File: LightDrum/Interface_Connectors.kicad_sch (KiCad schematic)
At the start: 6 parts, among them J1201 0525593652, J1202 0541323662, J1203 PWR-CONN

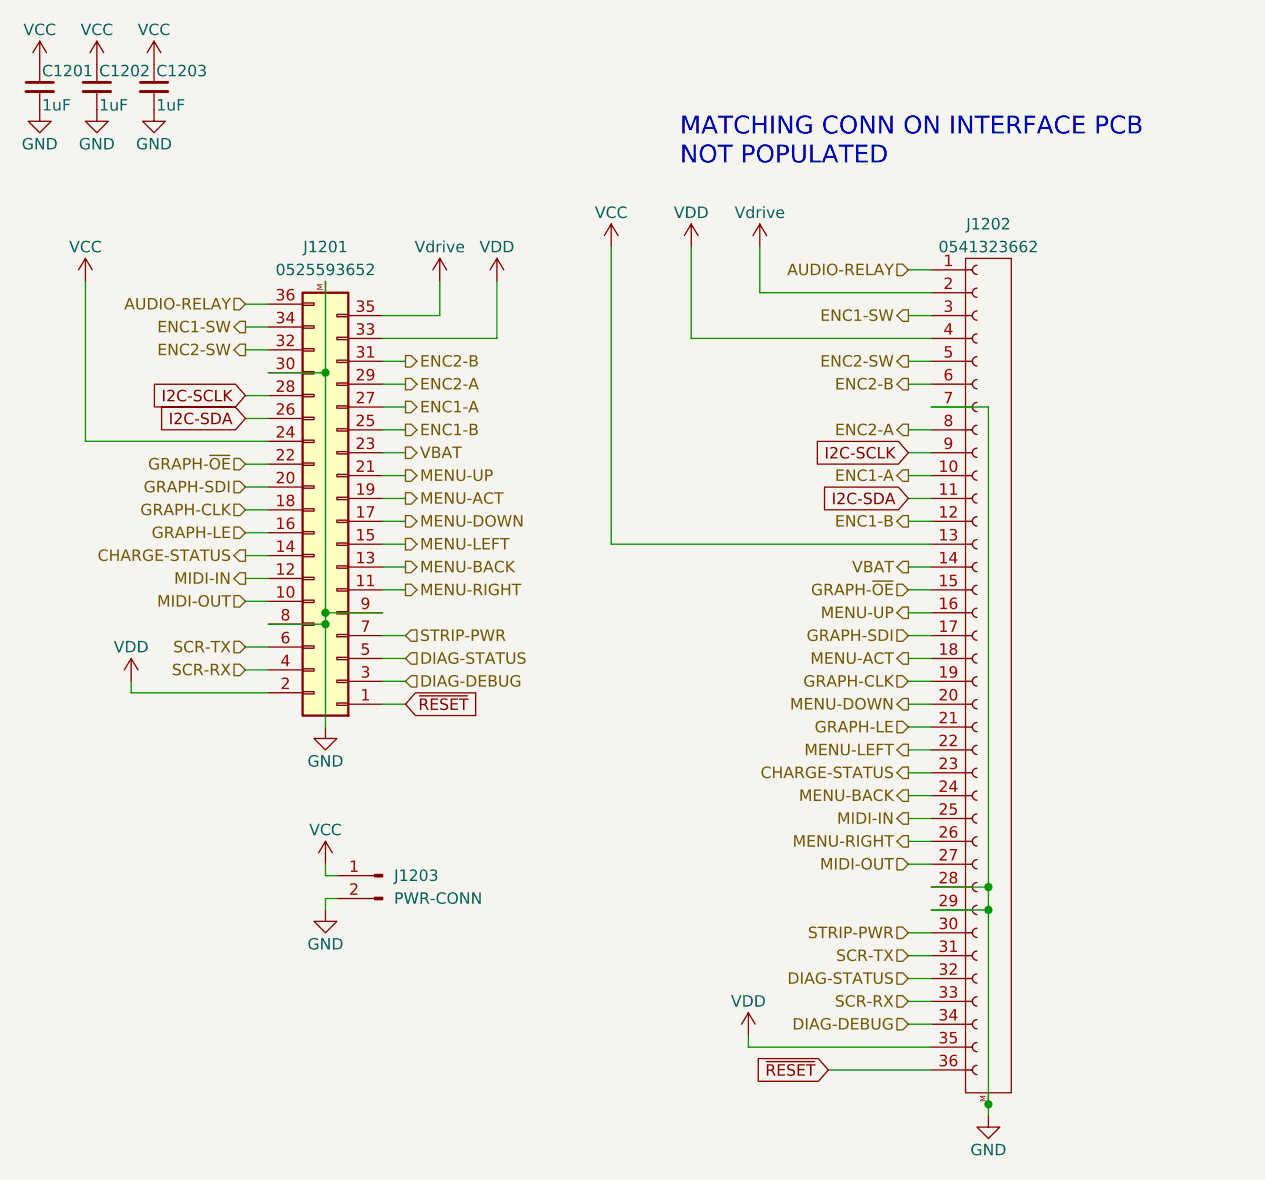
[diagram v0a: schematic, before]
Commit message: Simplify analog power supply and add some routing
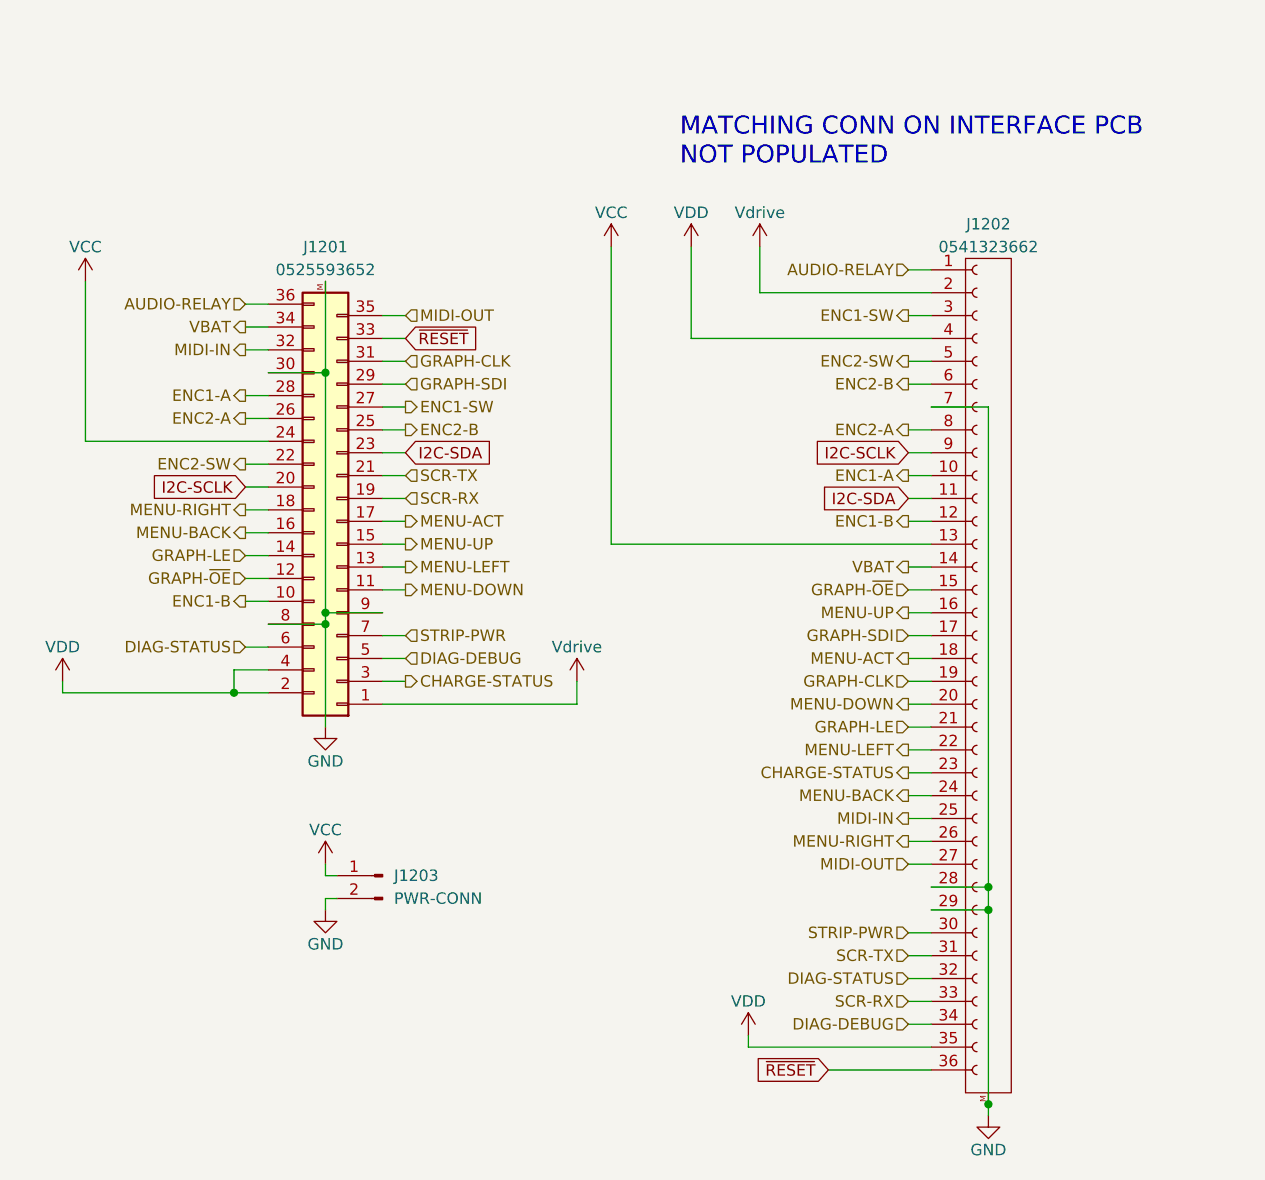
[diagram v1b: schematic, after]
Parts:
- removed C1201, C1202, C1203: 1uF, Capacitor_SMD:C_1206_3216Metric, symbol Device:C_Small
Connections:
- net CHARGE-STATUS: now also J1201.3 (Pin_3); no longer J1201.14 (Pin_14)
- net DIAG-DEBUG: now also J1201.5 (Pin_5); no longer J1201.3 (Pin_3)
- net DIAG-STATUS: now also J1201.6 (Pin_6); no longer J1201.5 (Pin_5)
- net ENC1-A: now also J1201.28 (Pin_28); no longer J1201.27 (Pin_27)
- net ENC1-B: now also J1201.10 (Pin_10); no longer J1201.25 (Pin_25)
- net ENC1-SW: now also J1201.27 (Pin_27); no longer J1201.34 (Pin_34)
- net ENC2-A: now also J1201.26 (Pin_26); no longer J1201.29 (Pin_29)
- net ENC2-B: now also J1201.25 (Pin_25); no longer J1201.31 (Pin_31)
- net ENC2-SW: now also J1201.22 (Pin_22); no longer J1201.32 (Pin_32)
- net GRAPH-CLK: now also J1201.31 (Pin_31); no longer J1201.18 (Pin_18)
- net GRAPH-LE: now also J1201.14 (Pin_14); no longer J1201.16 (Pin_16)
- net GRAPH-SDI: now also J1201.29 (Pin_29); no longer J1201.20 (Pin_20)
- net GRAPH-~{OE}: now also J1201.12 (Pin_12); no longer J1201.22 (Pin_22)
- net I2C-SCLK: now also J1201.20 (Pin_20); no longer J1201.28 (Pin_28)
- net I2C-SDA: now also J1201.23 (Pin_23); no longer J1201.26 (Pin_26)
- net MENU-ACT: now also J1201.17 (Pin_17); no longer J1201.19 (Pin_19)
- net MENU-BACK: now also J1201.16 (Pin_16); no longer J1201.13 (Pin_13)
- net MENU-DOWN: now also J1201.11 (Pin_11); no longer J1201.17 (Pin_17)
- net MENU-LEFT: now also J1201.13 (Pin_13); no longer J1201.15 (Pin_15)
- net MENU-RIGHT: now also J1201.18 (Pin_18); no longer J1201.11 (Pin_11)
- net MENU-UP: now also J1201.15 (Pin_15); no longer J1201.21 (Pin_21)
- net MIDI-IN: now also J1201.32 (Pin_32); no longer J1201.12 (Pin_12)
- net MIDI-OUT: now also J1201.35 (Pin_35); no longer J1201.10 (Pin_10)
- net SCR-RX: now also J1201.19 (Pin_19); no longer J1201.4 (Pin_4)
- net SCR-TX: now also J1201.21 (Pin_21); no longer J1201.6 (Pin_6)
- net VBAT: now also J1201.34 (Pin_34); no longer J1201.23 (Pin_23)
- net VDD: now also J1201.4 (Pin_4); no longer J1201.33 (Pin_33)
- net Vdrive: now also J1201.1 (Pin_1); no longer J1201.35 (Pin_35)
- net ~{RESET}: now also J1201.33 (Pin_33); no longer J1201.1 (Pin_1)

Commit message: Swap mcu again... (WIP)
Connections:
- net CHARGE-STATUS is gone; now on net GND: J1201.3 (Pin_3), J1202.23 (Pin_23)
- net VBAT is gone; now on net GND: J1201.34 (Pin_34), J1202.14 (Pin_14)
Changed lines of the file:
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@@
     (company "Daxxn Industries")
   )
+  (junction (at 124.46 99.06) (diameter 0) (color 0 0 0 0)
+  )
   (junction (at 40.64 90.17) (diameter 0) (color 0 0 0 0)
   )
@@
   (junction (at 50.8 54.61) (diameter 0) (color 0 0 0 0)
   )
+  (junction (at 124.46 76.2) (diameter 0) (color 0 0 0 0)
+  )
   (junction (at 124.46 135.89) (diameter 0) (color 0 0 0 0)
   )
+  (junction (at 50.8 49.53) (diameter 0) (color 0 0 0 0)
+  )
+  (junction (at 50.8 88.9) (diameter 0) (color 0 0 0 0)
+  )
   (junction (at 50.8 82.55) (diameter 0) (color 0 0 0 0)
   )
@@
     (stroke (width 0) (type default) (color 0 0 0 0))
   )
-  (wire (pts (xy 115.57 99.06) (xy 118.11 99.06))
+  (wire (pts (xy 50.8 88.9) (xy 50.8 93.98))
     (stroke (width 0) (type default) (color 0 0 0 0))
   )
@@
     (stroke (width 0) (type default) (color 0 0 0 0))
   )
-  (wire (pts (xy 118.11 76.2) (xy 115.57 76.2))
-    (stroke (width 0) (type default) (color 0 0 0 0))
-  )
   (wire (pts (xy 41.91 59.69) (xy 44.45 59.69))
     (stroke (width 0) (type default) (color 0 0 0 0))
@@
     (stroke (width 0) (type default) (color 0 0 0 0))
   )
+  (wire (pts (xy 50.8 88.9) (xy 57.15 88.9))
+    (stroke (width 0) (type default) (color 0 0 0 0))
+  )
+  (wire (pts (xy 44.45 49.53) (xy 50.8 49.53))
+    (stroke (width 0) (type default) (color 0 0 0 0))
+  )
   (wire (pts (xy 118.11 86.36) (xy 115.57 86.36))
     (stroke (width 0) (type default) (color 0 0 0 0))
@@
     (stroke (width 0) (type default) (color 0 0 0 0))
   )
-  (wire (pts (xy 41.91 49.53) (xy 44.45 49.53))
-    (stroke (width 0) (type default) (color 0 0 0 0))
-  )
   (wire (pts (xy 41.91 85.09) (xy 44.45 85.09))
     (stroke (width 0) (type default) (color 0 0 0 0))
@@
     (stroke (width 0) (type default) (color 0 0 0 0))
   )
-  (wire (pts (xy 124.46 58.42) (xy 124.46 111.76))
+  (wire (pts (xy 124.46 58.42) (xy 124.46 76.2))
     (stroke (width 0) (type default) (color 0 0 0 0))
   )
@@
     (stroke (width 0) (type default) (color 0 0 0 0))
   )
+  (wire (pts (xy 118.11 76.2) (xy 124.46 76.2))
+    (stroke (width 0) (type default) (color 0 0 0 0))
+  )
   (wire (pts (xy 118.11 121.92) (xy 115.57 121.92))
     (stroke (width 0) (type default) (color 0 0 0 0))
@@
     (stroke (width 0) (type default) (color 0 0 0 0))
   )
-  (wire (pts (xy 50.8 82.55) (xy 50.8 93.98))
+  (wire (pts (xy 50.8 82.55) (xy 50.8 88.9))
     (stroke (width 0) (type default) (color 0 0 0 0))
   )
@@
     (stroke (width 0) (type default) (color 0 0 0 0))
   )
+  (wire (pts (xy 124.46 99.06) (xy 124.46 111.76))
+    (stroke (width 0) (type default) (color 0 0 0 0))
+  )
   (wire (pts (xy 40.64 87.63) (xy 40.64 90.17))
     (stroke (width 0) (type default) (color 0 0 0 0))
   )
+  (wire (pts (xy 118.11 99.06) (xy 124.46 99.06))
+    (stroke (width 0) (type default) (color 0 0 0 0))
+  )
   (wire (pts (xy 97.79 128.27) (xy 97.79 129.54))
     (stroke (width 0) (type default) (color 0 0 0 0))
@@
     (stroke (width 0) (type default) (color 0 0 0 0))
   )
-  (wire (pts (xy 57.15 88.9) (xy 59.69 88.9))
-    (stroke (width 0) (type default) (color 0 0 0 0))
-  )
   (wire (pts (xy 118.11 45.72) (xy 99.06 45.72))
     (stroke (width 0) (type default) (color 0 0 0 0))
@@
     (stroke (width 0) (type default) (color 0 0 0 0))
   )
+  (wire (pts (xy 124.46 76.2) (xy 124.46 99.06))
+    (stroke (width 0) (type default) (color 0 0 0 0))
+  )
   (wire (pts (xy 50.8 81.28) (xy 50.8 82.55))
     (stroke (width 0) (type default) (color 0 0 0 0))
@@
     (stroke (width 0) (type default) (color 0 0 0 0))
   )
-  (wire (pts (xy 50.8 44.45) (xy 50.8 54.61))
+  (wire (pts (xy 50.8 44.45) (xy 50.8 49.53))
     (stroke (width 0) (type default) (color 0 0 0 0))
   )
@@
   )
   (wire (pts (xy 41.91 67.31) (xy 44.45 67.31))
+    (stroke (width 0) (type default) (color 0 0 0 0))
+  )
+  (wire (pts (xy 50.8 49.53) (xy 50.8 54.61))
     (stroke (width 0) (type default) (color 0 0 0 0))
   )
@@
     (effects (font (size 2 2)) (justify left bottom))
   )
-  (global_label "I2C-SCLK" (shape input) (at 115.57 63.5 180) (fields_autoplaced)
-    (effects (font (size 1.27 1.27)) (justify right))
-    (property "Intersheet References" "${INTERSHEET_REFS}" (id 0) (at 103.7226 63.4206 0)
-      (effects (font (size 1.27 1.27)) (justify right) hide)
-    )
-  )
-  (global_label "~{RESET}" (shape input) (at 106.68 132.08 180) (fields_autoplaced)
-    (effects (font (size 1.27 1.27)) (justify right))
-    (property "Intersheet References" "${INTERSHEET_REFS}" (id 0) (at 98.5217 132.0006 0)
-      (effects (font (size 1.27 1.27)) (justify right) hide)
-    )
-  )
-  (global_label "~{RESET}" (shape input) (at 59.69 50.8 0) (fields_autoplaced)
-    (effects (font (size 1.27 1.27)) (justify left))
-    (property "Intersheet References" "${INTERSHEET_REFS}" (id 0) (at 67.8483 50.8794 0)
-      (effects (font (size 1.27 1.27)) (justify left) hide)
-    )
-  )
-  (global_label "I2C-SDA" (shape input) (at 115.57 68.58 180) (fields_autoplaced)
-    (effects (font (size 1.27 1.27)) (justify right))
-    (property "Intersheet References" "${INTERSHEET_REFS}" (id 0) (at 104.9321 68.5006 0)
-      (effects (font (size 1.27 1.27)) (justify right) hide)
-    )
-  )
-  (global_label "I2C-SDA" (shape input) (at 59.69 63.5 0) (fields_autoplaced)
-    (effects (font (size 1.27 1.27)) (justify left))
-    (property "Intersheet References" "${INTERSHEET_REFS}" (id 0) (at 70.3279 63.5794 0)
-      (effects (font (size 1.27 1.27)) (justify left) hide)
-    )
-  )
-  (global_label "I2C-SCLK" (shape input) (at 41.91 67.31 180) (fields_autoplaced)
-    (effects (font (size 1.27 1.27)) (justify right))
-    (property "Intersheet References" "${INTERSHEET_REFS}" (id 0) (at 30.0626 67.2306 0)
-      (effects (font (size 1.27 1.27)) (justify right) hide)
-    )
-  )
   (hierarchical_label "AUDIO-RELAY" (shape input) (at 115.57 43.18 180)
     (effects (font (size 1.27 1.27)) (justify right))
@@
     (effects (font (size 1.27 1.27)) (justify left))
   )
-  (hierarchical_label "CHARGE-STATUS" (shape output) (at 115.57 99.06 180)
-    (effects (font (size 1.27 1.27)) (justify right))
-  )
   (hierarchical_label "MENU-BACK" (shape output) (at 115.57 101.6 180)
     (effects (font (size 1.27 1.27)) (justify right))
@@
     (effects (font (size 1.27 1.27)) (justify right))
   )
-  (hierarchical_label "CHARGE-STATUS" (shape output) (at 59.69 88.9 0)
-    (effects (font (size 1.27 1.27)) (justify left))
-  )
   (hierarchical_label "MENU-UP" (shape output) (at 115.57 81.28 180)
     (effects (font (size 1.27 1.27)) (justify right))
@@
     (effects (font (size 1.27 1.27)) (justify right))
   )
-  (hierarchical_label "VBAT" (shape output) (at 41.91 49.53 180)
-    (effects (font (size 1.27 1.27)) (justify right))
-  )
   (hierarchical_label "ENC1-SW" (shape output) (at 115.57 48.26 180)
     (effects (font (size 1.27 1.27)) (justify right))
@@
     (effects (font (size 1.27 1.27)) (justify right))
   )
+  (hierarchical_label "I2C-SDA" (shape input) (at 115.57 68.58 180)
+    (effects (font (size 1.27 1.27)) (justify right))
+  )
   (hierarchical_label "SCR-RX" (shape input) (at 59.69 68.58 0)
     (effects (font (size 1.27 1.27)) (justify left))
@@
     (effects (font (size 1.27 1.27)) (justify right))
   )
+  (hierarchical_label "I2C-SCLK" (shape input) (at 41.91 67.31 180)
+    (effects (font (size 1.27 1.27)) (justify right))
+  )
   (hierarchical_label "SCR-TX" (shape input) (at 115.57 119.38 180)
     (effects (font (size 1.27 1.27)) (justify right))
@@
     (effects (font (size 1.27 1.27)) (justify left))
   )
+  (hierarchical_label "~{RESET}" (shape input) (at 106.68 132.08 180)
+    (effects (font (size 1.27 1.27)) (justify right))
+  )
   (hierarchical_label "MENU-BACK" (shape output) (at 41.91 72.39 180)
     (effects (font (size 1.27 1.27)) (justify right))
@@
     (effects (font (size 1.27 1.27)) (justify right))
   )
+  (hierarchical_label "I2C-SCLK" (shape input) (at 115.57 63.5 180)
+    (effects (font (size 1.27 1.27)) (justify right))
+  )
   (hierarchical_label "ENC2-B" (shape output) (at 59.69 60.96 0)
     (effects (font (size 1.27 1.27)) (justify left))
@@
     (effects (font (size 1.27 1.27)) (justify right))
   )
+  (hierarchical_label "I2C-SDA" (shape input) (at 59.69 63.5 0)
+    (effects (font (size 1.27 1.27)) (justify left))
+  )
   (hierarchical_label "MENU-UP" (shape output) (at 59.69 73.66 0)
     (effects (font (size 1.27 1.27)) (justify left))
   )
-  (hierarchical_label "VBAT" (shape output) (at 115.57 76.2 180)
-    (effects (font (size 1.27 1.27)) (justify right))
-  )
   (hierarchical_label "SCR-TX" (shape input) (at 59.69 66.04 0)
     (effects (font (size 1.27 1.27)) (justify left))
@@
     (effects (font (size 1.27 1.27)) (justify right))
   )
+  (hierarchical_label "~{RESET}" (shape input) (at 59.69 50.8 0)
+    (effects (font (size 1.27 1.27)) (justify left))
+  )
   (hierarchical_label "GRAPH-CLK" (shape input) (at 115.57 88.9 180)

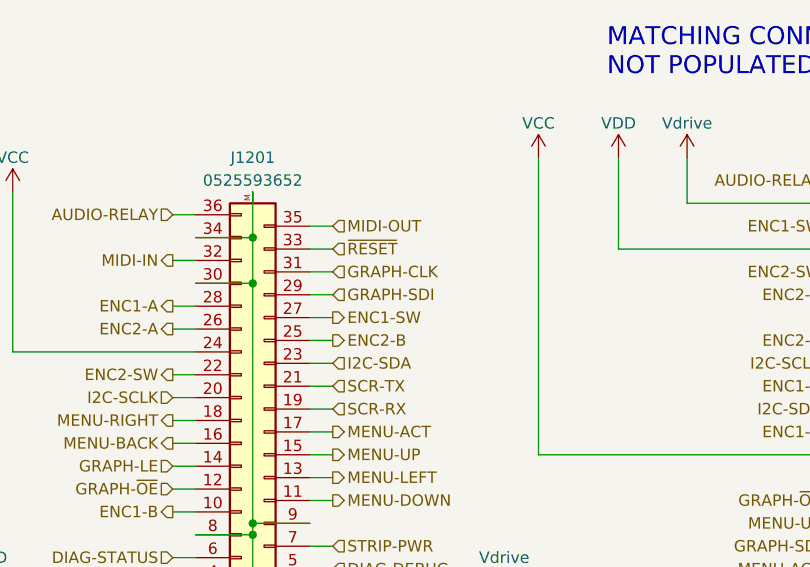
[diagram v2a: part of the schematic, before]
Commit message: Replace barrel jacks with proper DIN4 conn and more
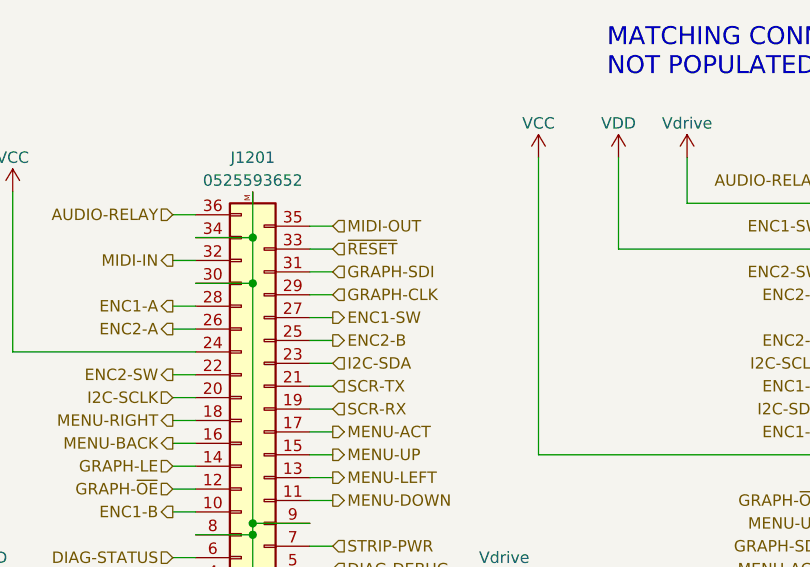
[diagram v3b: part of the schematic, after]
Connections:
- net GRAPH-CLK: now also J1201.29 (Pin_29); no longer J1201.31 (Pin_31)
- net GRAPH-SDI: now also J1201.31 (Pin_31); no longer J1201.29 (Pin_29)
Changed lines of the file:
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@@
     (effects (font (size 1.27 1.27)) (justify right))
   )
-  (hierarchical_label "GRAPH-CLK" (shape input) (at 59.69 53.34 0)
+  (hierarchical_label "GRAPH-CLK" (shape input) (at 59.69 55.88 0)
     (effects (font (size 1.27 1.27)) (justify left))
   )
@@
     (effects (font (size 1.27 1.27)) (justify left))
   )
-  (hierarchical_label "GRAPH-SDI" (shape input) (at 59.69 55.88 0)
+  (hierarchical_label "GRAPH-SDI" (shape input) (at 59.69 53.34 0)
     (effects (font (size 1.27 1.27)) (justify left))
   )
